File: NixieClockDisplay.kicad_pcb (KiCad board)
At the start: 2 copper layers, 160 x 65 mm, 55 parts, among them J1 CONN_01X08, J2 CONN_01X03, J3 CONN_01X03, U1 TPIC6B595, U2 TPIC6B595, U3 TPIC6B595, U4 TPIC6B595, U5 TPIC6B595, U6 TPIC6B595, U7 WE-FDSM_DC/DC_5V

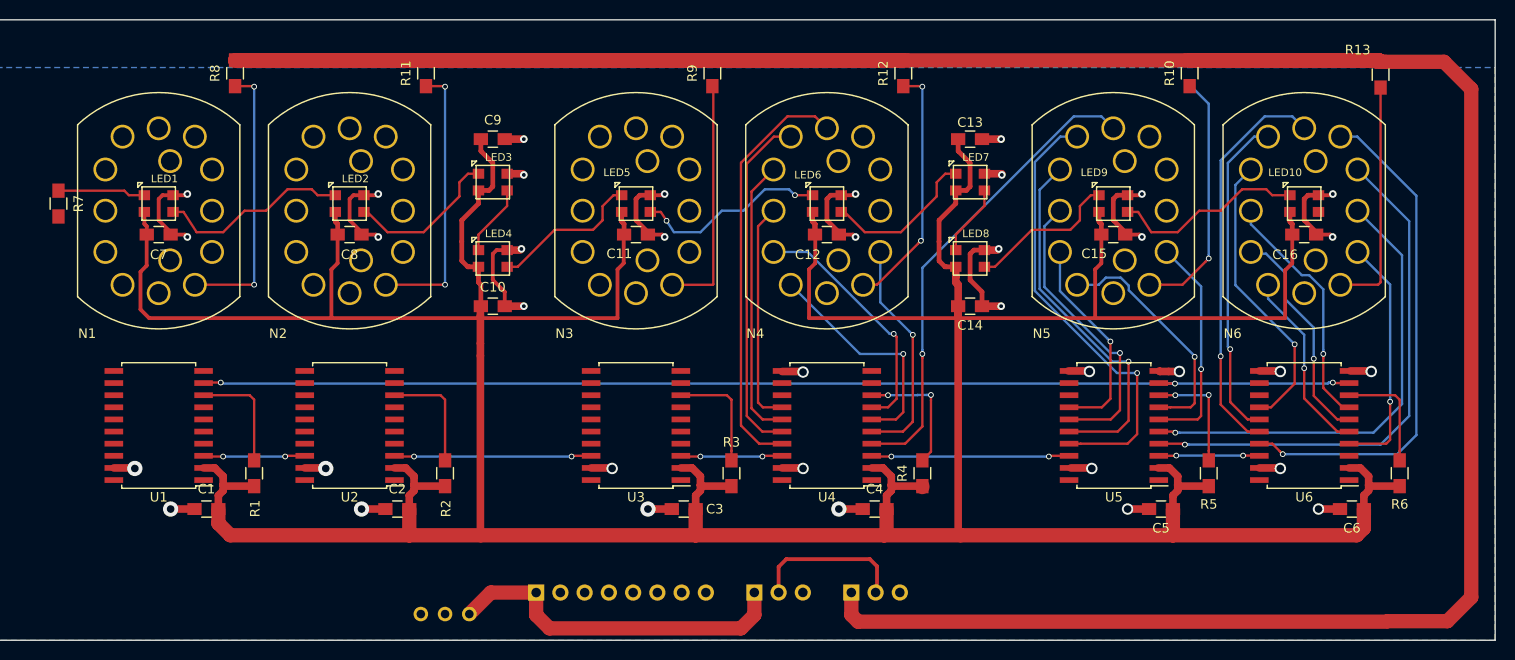
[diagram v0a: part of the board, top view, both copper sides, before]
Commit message: Rotated driver chips
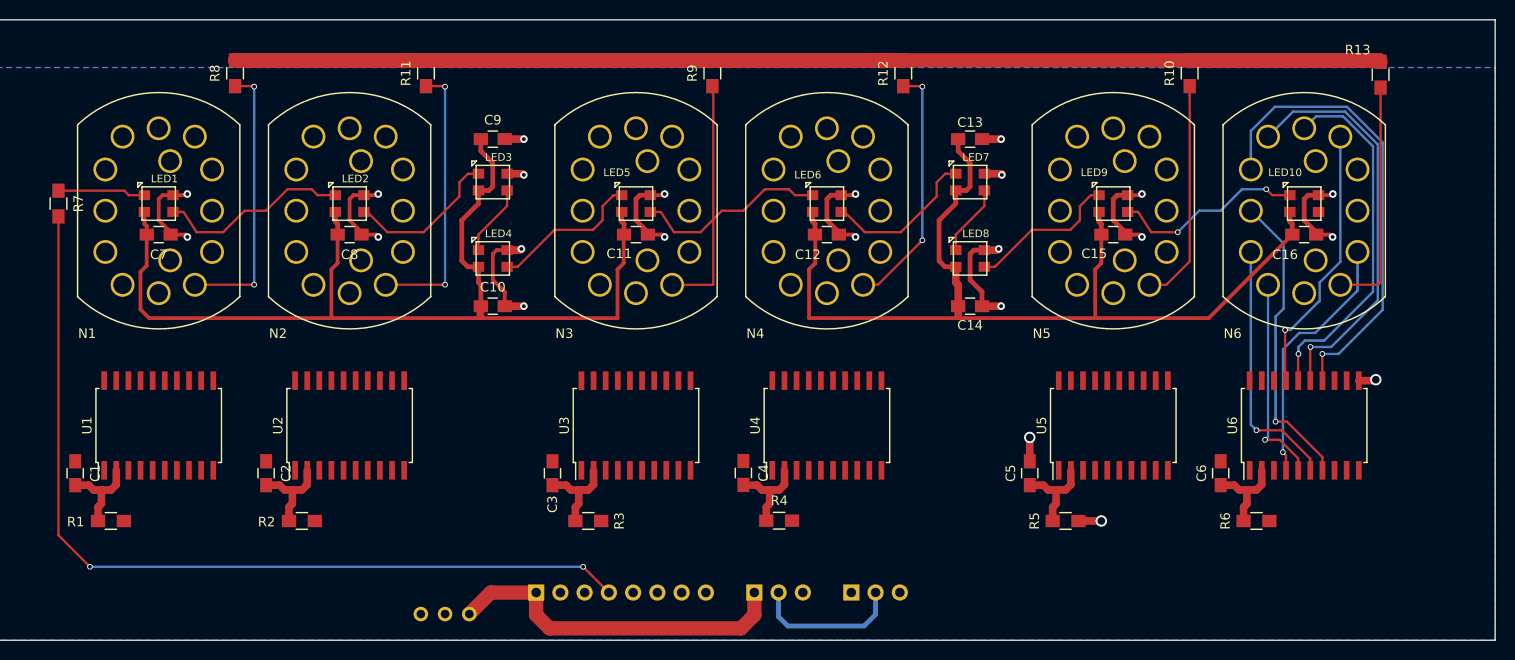
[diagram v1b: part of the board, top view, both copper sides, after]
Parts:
- moved R1 15.8 mm to (85.0, 92.5), turned to 0 degrees
- moved R2 15.8 mm to (105.0, 92.5), turned to 0 degrees
- moved R3 15.8 mm to (135.0, 92.5), turned to 0 degrees
- moved R5 15.8 mm to (185.0, 92.5), turned to 0 degrees
- moved R6 15.8 mm to (205.0, 92.5), turned to 0 degrees
- moved R4 15.8 mm to (155.0, 92.5), turned to 0 degrees
- moved C4 14.3 mm to (151.2, 87.5), turned to 270 degrees
- moved C1 14.3 mm to (81.2, 87.5), turned to 270 degrees
- moved C2 14.3 mm to (101.2, 87.5), turned to 270 degrees
- moved C3 14.3 mm to (131.2, 87.5), turned to 270 degrees
- moved C5 14.3 mm to (181.2, 87.5), turned to 270 degrees
- moved C6 14.3 mm to (201.2, 87.5), turned to 270 degrees
- moved U5 0.07 mm to (190.0, 82.5), turned to 90 degrees
- turned U1 to 90 degrees
- turned U2 to 90 degrees
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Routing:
- net +5V: track 456.8 -> 268.5 mm
- net /HV: track 342.3 -> 209.9 mm
- net //G: track 121.9 -> 0.00 mm, vias 3 -> 0
- net /PIXEL_IN: track 0.00 -> 93.5 mm, vias 0 -> 2
- net /SEC_8: track 56.1 -> 0.00 mm, vias 1 -> 0
- net /SEC_60: track 49.8 -> 0.00 mm, vias 1 -> 0
- net /SEC_9: track 49.2 -> 0.00 mm, vias 1 -> 0
- net /SEC_50: track 47.3 -> 0.00 mm, vias 1 -> 0
- net /MIN_6: track 44.2 -> 0.00 mm
- net /SEC_40: track 38.8 -> 0.00 mm, vias 1 -> 0
- net /MIN_5: track 36.6 -> 0.00 mm
- net GND: track 123.7 -> 90.2 mm, vias 37 -> 22
- net /SEC_30: track 31.2 -> 0.00 mm, vias 1 -> 0
- net /MIN_4: track 29.7 -> 0.00 mm
- net /MIN_2: track 27.6 -> 0.00 mm, vias 1 -> 0
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
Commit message: Near complete layout
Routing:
- net +5V: track 268.5 -> 460.2 mm, vias 0 -> 9
- net /SRCK: track 0.00 -> 182.4 mm, vias 0 -> 8
- net /RCK: track 0.00 -> 162.0 mm, vias 0 -> 8
- net //G: track 0.00 -> 151.0 mm, vias 0 -> 6
- net /HV: track 209.9 -> 330.5 mm
- net /MIN_9: track 0.00 -> 81.0 mm, vias 0 -> 2
- net /HOUR_9: track 0.00 -> 78.5 mm, vias 0 -> 2
- net /MIN_8: track 0.00 -> 75.5 mm, vias 0 -> 2
- net Net-(J1-Pad8): track 0.00 -> 71.1 mm, vias 0 -> 1
- net /HOUR_8: track 0.00 -> 70.4 mm, vias 0 -> 2
- net /MIN_7: track 0.00 -> 69.6 mm, vias 0 -> 2
- net /SEC_60: track 0.00 -> 65.6 mm, vias 0 -> 2
- net /HOUR_7: track 0.00 -> 64.4 mm, vias 0 -> 2
- net /MIN_50: track 0.00 -> 54.4 mm, vias 0 -> 2
- net /SEC_8: track 0.00 -> 50.6 mm
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
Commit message: Routing complete
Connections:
- J3 pad 2: /SHDN -> Net-(J3-Pad2)
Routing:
- net //G: track 151.0 -> 165.8 mm
- net /SHDN: track 15.9 -> 26.1 mm
- net Net-(N5-Pad1): track 27.9 -> 25.0 mm
- net /HOUR_00: track 29.6 -> 27.3 mm
- net /HOUR_9: track 78.5 -> 76.3 mm
- net GND: track 138.4 -> 140.6 mm
- net /SEC_50: track 36.5 -> 35.0 mm
- net /SEC_40: track 31.2 -> 29.8 mm
- net Net-(N1-Pad1): track 25.9 -> 25.0 mm
- net /SEC_30: track 27.0 -> 26.2 mm
- net /HOUR_8: track 70.4 -> 69.8 mm
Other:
- board text added: "+12V"
- board text added: "DATA IN"
- board text added: "ENABLE"
- board text added: "GND"
- board text added: "HV+"
- board text added: "HV-"
- board text added: "PIXEL IN"
- board text added: "RCK"
- board text added: "SHDN"
- board text added: "SRCK"

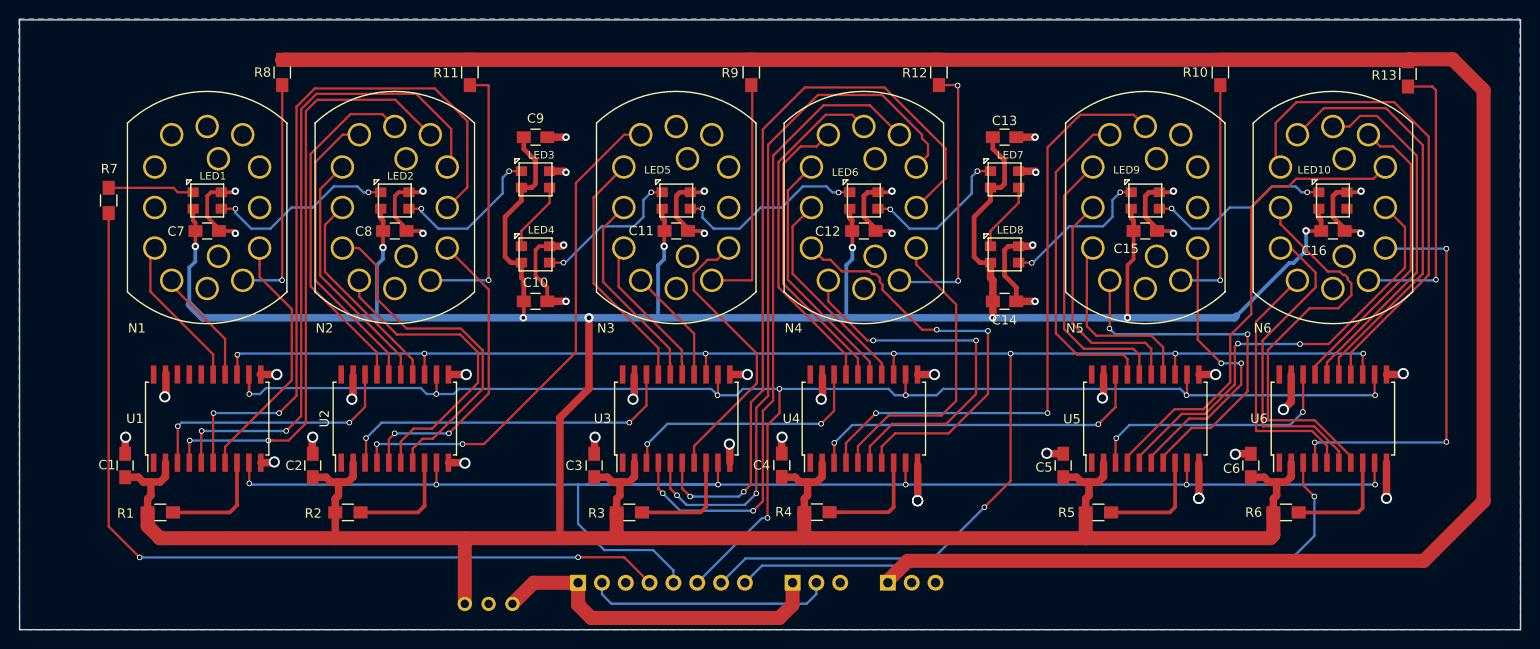
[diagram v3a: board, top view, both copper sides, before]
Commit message: Added mounting holes
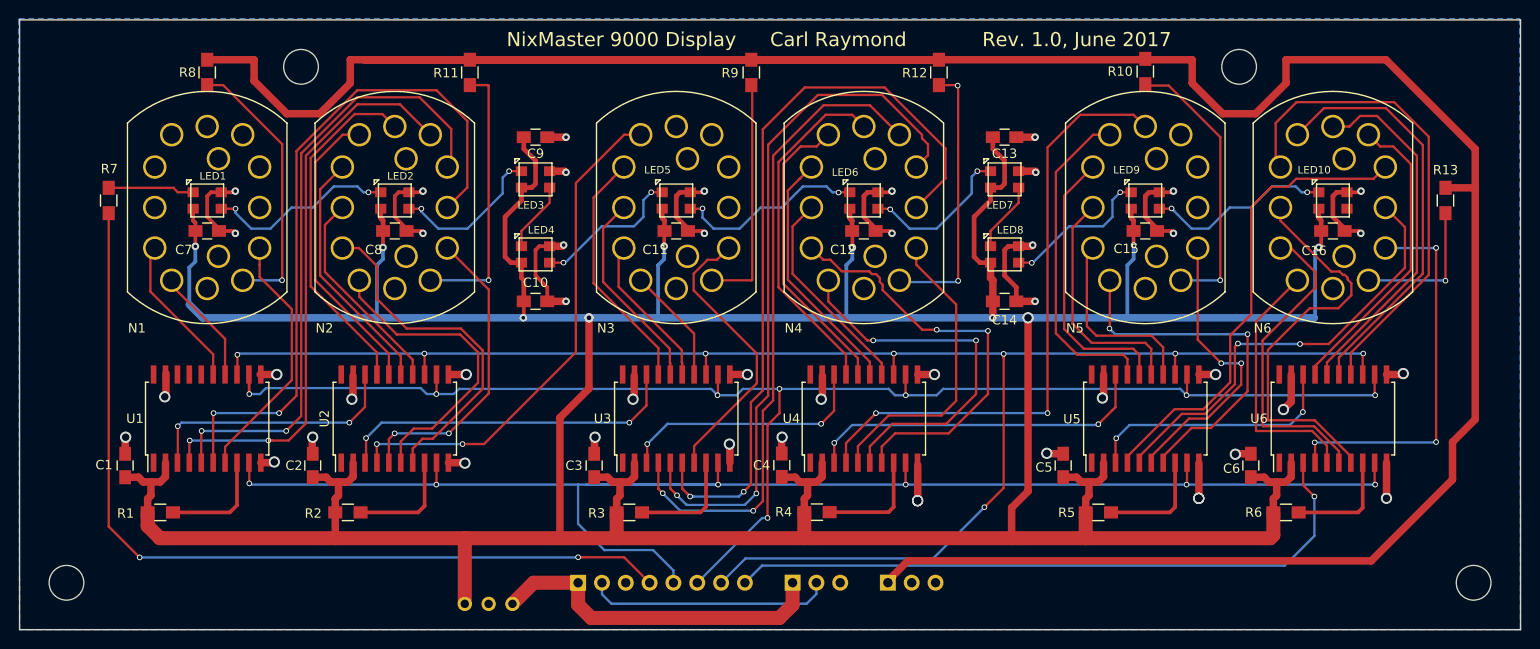
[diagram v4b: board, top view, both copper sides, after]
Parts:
- added REF**: MountingHole_3.7mm, Mounting_Holes:MountingHole_3.7mm, F.Cu at (225.0, 100.0)
- added REF**: MountingHole_3.7mm, Mounting_Holes:MountingHole_3.7mm, F.Cu at (75.0, 100.0)
- added REF**: MountingHole_3.7mm, Mounting_Holes:MountingHole_3.7mm, F.Cu at (100.0, 45.0)
- added REF**: MountingHole_3.7mm, Mounting_Holes:MountingHole_3.7mm, F.Cu at (200.0, 45.0)
- J1: footprint Pin_Headers:Pin_Header_Angled_1x08_Pitch2.54mm -> Pin_Headers:Pin_Header_Straight_1x08_Pitch2.54mm
- J2, J3: footprint Pin_Headers:Pin_Header_Angled_1x03_Pitch2.54mm -> Pin_Headers:Pin_Header_Straight_1x03_Pitch2.54mm
- moved R13 14.1 mm to (222.0, 59.2)
- moved R10 8.00 mm to (190.0, 45.5)
- moved R8 8.00 mm to (90.0, 45.6)
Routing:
- net +5V: track 460.6 -> 488.3 mm, vias 9 -> 10
- net Net-(N6-Pad1): track 30.6 -> 15.4 mm
- net /HV: track 330.5 -> 320.0 mm
- net Net-(N5-Pad1): track 25.0 -> 29.7 mm
- net Net-(N1-Pad1): track 25.0 -> 29.3 mm
- net /HOUR_7: track 64.1 -> 60.9 mm
- net /HOUR_8: track 69.8 -> 66.8 mm
- net /HOUR_9: track 76.3 -> 73.4 mm
- net /SEC_0: track 43.4 -> 41.2 mm
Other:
- board text added: "Carl Raymond"
- board text added: "NixMaster 9000 Display"
- board text added: "Rev. 1.0, June 2017"

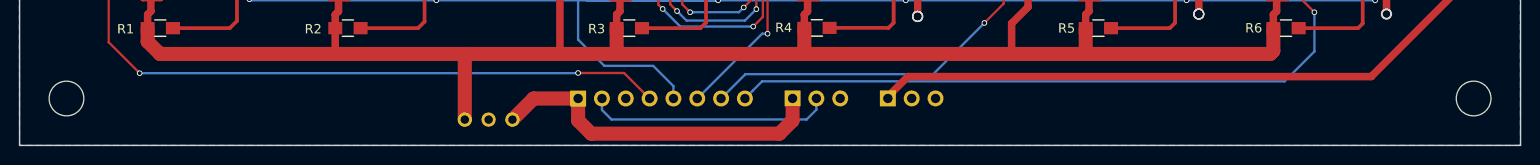
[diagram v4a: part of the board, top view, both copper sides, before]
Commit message: Moved mounting holes
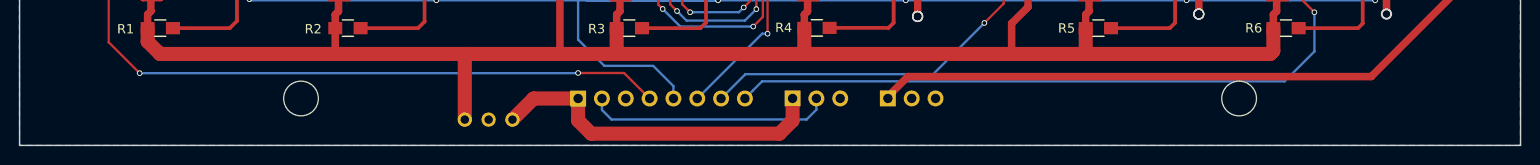
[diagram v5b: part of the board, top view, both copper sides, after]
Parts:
- moved REF** 25.0 mm to (200.0, 100.0)
- moved REF** 25.0 mm to (100.0, 100.0)
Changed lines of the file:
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@@
   (general
     (links 187)
-    (no_connects 0)
-    (area 66.071429 -19.850392 233.928572 140.350392)
+    (no_connects 1)
+    (area 69.924999 39.924999 230.075001 105.075001)
     (thickness 1.6)
     (drawings 22)
@@
   )
   (setup
-    (last_trace_width 0.8)
+    (last_trace_width 0.25)
     (user_trace_width 0.4)
     (user_trace_width 0.5)
@@
     (mod_text_size 1 1)
     (mod_text_width 0.15)
-    (pad_size 1.524 1.524)
-    (pad_drill 0.762)
+    (pad_size 3.7 3.7)
+    (pad_drill 3.7)
     (pad_to_mask_clearance 0.2)
     (aux_axis_origin 0 0)
@@
   )
   (module Mounting_Holes:MountingHole_3.7mm (layer F.Cu)
-    (at 225 100)
+    (at 200 100)
     (descr "Mounting Hole 3.7mm, no annular")
     (tags "mounting hole 3.7mm no annular")
@@
   )
   (module Mounting_Holes:MountingHole_3.7mm (layer F.Cu)
-    (at 75 100)
+    (at 100 100)
     (descr "Mounting Hole 3.7mm, no annular")
     (tags "mounting hole 3.7mm no annular")

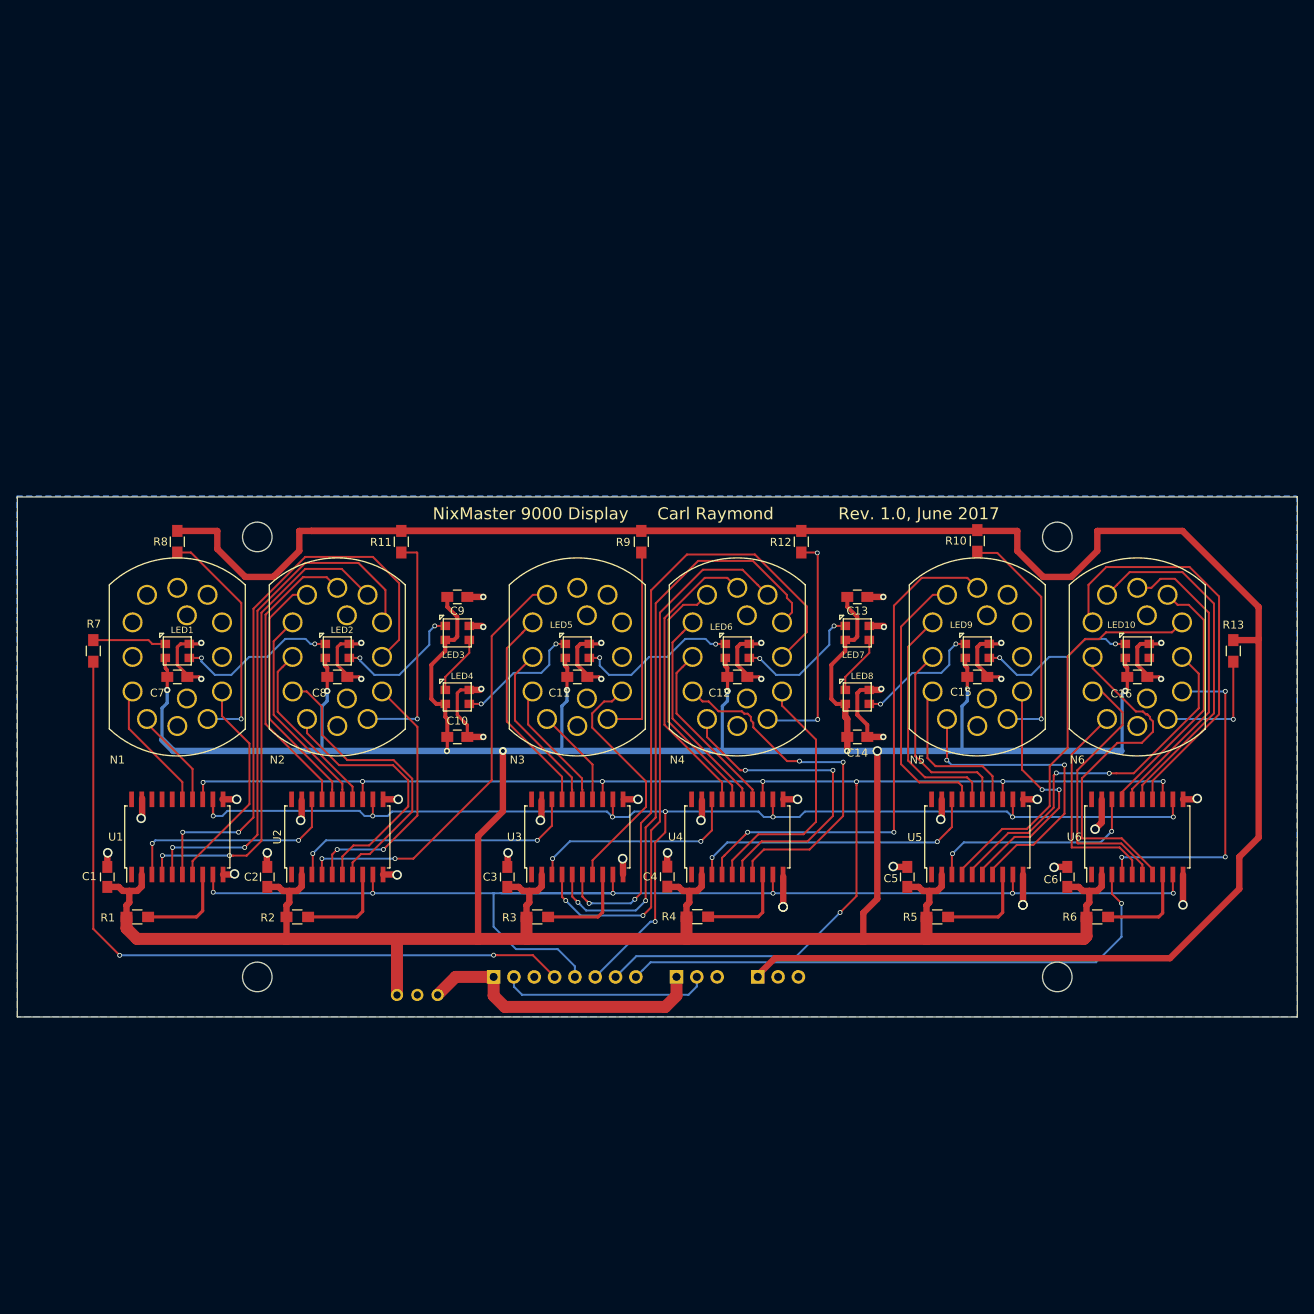
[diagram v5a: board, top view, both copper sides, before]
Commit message: Moved tracks away from mounting holes
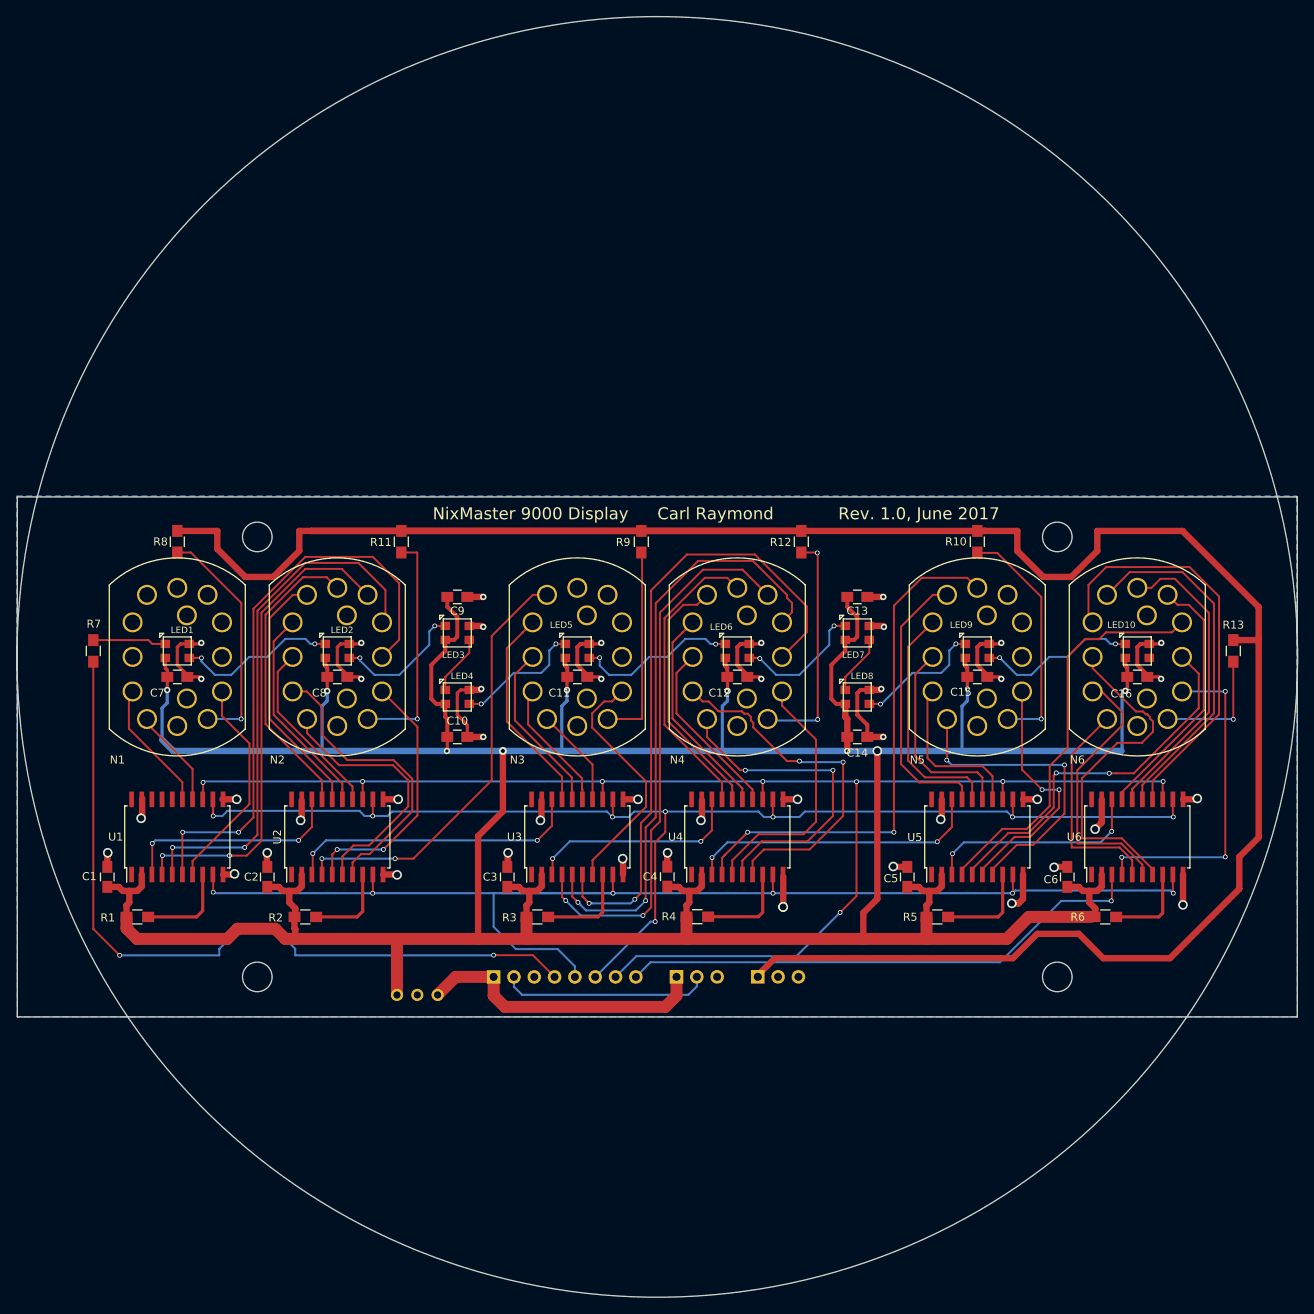
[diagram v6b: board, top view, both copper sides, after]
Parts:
- moved R2 1.00 mm to (106.0, 92.5)
- moved R6 1.00 mm to (206.0, 92.5)
- moved R10 0.10 mm to (190.0, 45.6)
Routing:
- net Net-(J1-Pad8): track 71.1 -> 66.7 mm
- net /HV: track 320.0 -> 323.5 mm
- net /PIXEL_IN: track 93.6 -> 97.0 mm
- net Net-(R6-Pad2): track 11.8 -> 10.9 mm
- net Net-(R2-Pad2): track 11.7 -> 10.8 mm
- net GND: track 140.6 -> 141.5 mm, vias 46 -> 45
- net +5V: track 488.3 -> 488.9 mm
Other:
- board size 160 x 65 mm -> 160.1 x 160.1 mm
